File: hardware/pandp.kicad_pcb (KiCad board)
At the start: 2 copper layers, 116 x 55.5 mm, 93 parts, among them IC1 ADP2303-5, IC2 DRV8830, P1 CONN_01X02, P10 CONN_01X04, P11 CONN_01X02, P12 CONN_02X04, P13 CONN_01X02, P14 CONN_01X04, P15 CONN_01X04, P16 CONN_01X03, P17 CONN_01X03, P18 CONN_01X03, P19 CONN_01X03, P2 CONN_01X03, P20 CONN_01X03, P21 CONN_01X03, P22 CONN_02X03, P23 CONN_02X03, P24 CONN_02X03, P25 CONN_02X03, P26 CONN_01X03, P27 CONN_01X03, P28 CONN_01X03, P29 CONN_01X03, P3 CONN_01X02, P30 CONN_01X04, P31 CONN_01X04, P32 CONN_01X04, P33 CONN_01X04, P4 CONN_01X03, P5 CONN_01X02, P6 CONN_01X03, P7 CONN_01X03, P8 USB_OTG, P9 CONN_01X02, Q1 IRF540N, Q2 IRF540N, SW1 SW_PUSH, U1 AP1117D33, U2 STM32F103RC, Y1 Crystal_Small - 2101357 on el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, Y2 Crystal_Small - 2063972 on el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

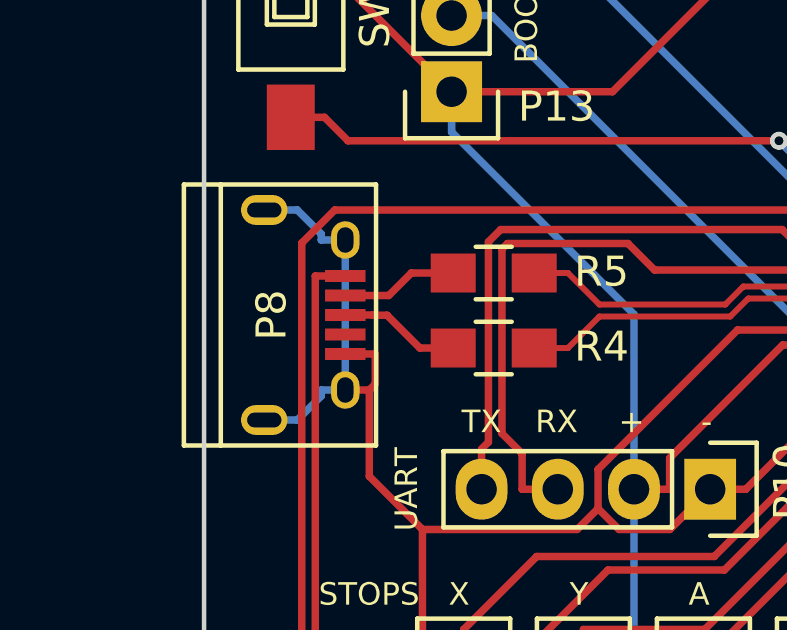
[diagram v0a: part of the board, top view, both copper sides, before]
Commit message: oshpark compatible holes for uusb connector
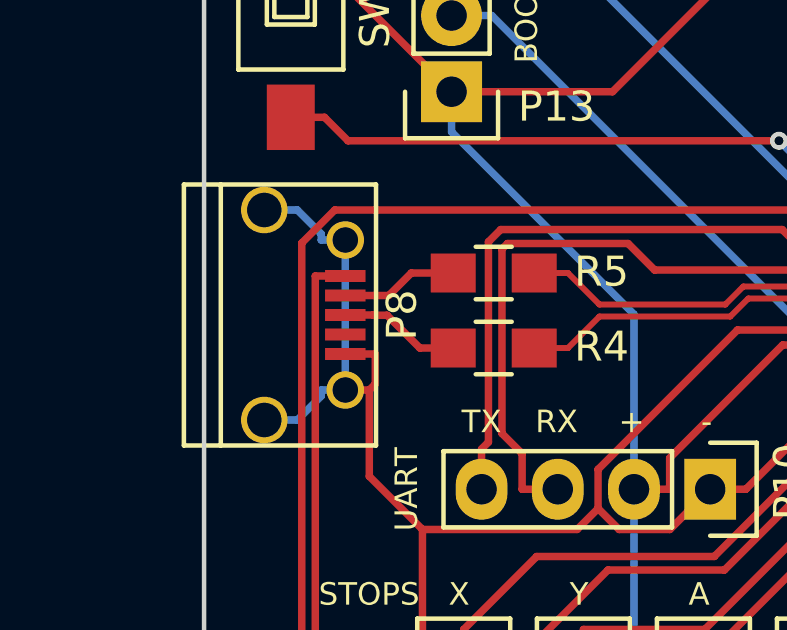
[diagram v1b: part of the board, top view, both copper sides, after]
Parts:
- P8: footprint Connect:USB_Micro-B -> MyLibs:USB_Micro-B-OshPark
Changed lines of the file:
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@@
     (links 267)
     (no_connects 0)
-    (area 82.424999 61.674999 198.575001 117.325001)
+    (area 77.775 50.367857 210.5 124.100001)
     (thickness 1.6)
     (drawings 78)
@@
     (36 B.SilkS user)
     (37 F.SilkS user)
-    (38 B.Mask user)
-    (39 F.Mask user)
+    (38 B.Mask user hide)
+    (39 F.Mask user hide)
     (40 Dwgs.User user)
     (41 Cmts.User user)
@@
     (add_net "Net-(IC2-Pad3)")
   )
-  (module Connect:USB_Micro-B (layer F.Cu)
-    (at 85.6447 97.693 270)
-    (descr "Micro USB Type B Receptacle")
-    (tags "USB USB_B USB_micro USB_OTG")
-    (attr smd)
-    (fp_text reference P8 (at 0 0.8947 270) (layer F.SilkS)
-      (effects (font (size 1 1) (thickness 0.15)))
-    )
-    (fp_text value USB_OTG (at 0 4.8 270) (layer F.Fab)
-      (effects (font (size 1 1) (thickness 0.15)))
-    )
-    (fp_line (start -4.6 -2.8) (end 4.6 -2.8) (layer F.CrtYd) (width 0.05))
-    (fp_line (start 4.6 -2.8) (end 4.6 4.05) (layer F.CrtYd) (width 0.05))
-    (fp_line (start 4.6 4.05) (end -4.6 4.05) (layer F.CrtYd) (width 0.05))
-    (fp_line (start -4.6 4.05) (end -4.6 -2.8) (layer F.CrtYd) (width 0.05))
-    (fp_line (start -4.3509 3.81746) (end 4.3491 3.81746) (layer F.SilkS) (width 0.15))
-    (fp_line (start -4.3509 -2.58754) (end 4.3491 -2.58754) (layer F.SilkS) (width 0.15))
-    (fp_line (start 4.3491 -2.58754) (end 4.3491 3.81746) (layer F.SilkS) (width 0.15))
-    (fp_line (start 4.3491 2.58746) (end -4.3509 2.58746) (layer F.SilkS) (width 0.15))
-    (fp_line (start -4.3509 3.81746) (end -4.3509 -2.58754) (layer F.SilkS) (width 0.15))
-    (pad 1 smd rect (at -1.3009 -1.56254) (size 1.35 0.4) (layers F.Cu F.Paste F.Mask)
-      (net 92 +5VL))
-    (pad 2 smd rect (at -0.6509 -1.56254) (size 1.35 0.4) (layers F.Cu F.Paste F.Mask)
-      (net 60 "Net-(P8-Pad2)"))
-    (pad 3 smd rect (at -0.0009 -1.56254) (size 1.35 0.4) (layers F.Cu F.Paste F.Mask)
-      (net 61 "Net-(P8-Pad3)"))
-    (pad 4 smd rect (at 0.6491 -1.56254) (size 1.35 0.4) (layers F.Cu F.Paste F.Mask))
-    (pad 5 smd rect (at 1.2991 -1.56254) (size 1.35 0.4) (layers F.Cu F.Paste F.Mask)
-      (net 90 GNDD))
-    (pad 6 thru_hole oval (at -2.5009 -1.56254) (size 0.95 1.25) (drill oval 0.55 0.85) (layers *.Cu *.Mask F.SilkS)
-      (net 90 GNDD))
-    (pad 6 thru_hole oval (at 2.4991 -1.56254) (size 0.95 1.25) (drill oval 0.55 0.85) (layers *.Cu *.Mask F.SilkS)
-      (net 90 GNDD))
-    (pad 6 thru_hole oval (at -3.5009 1.13746) (size 1.55 1) (drill oval 1.15 0.5) (layers *.Cu *.Mask F.SilkS)
-      (net 90 GNDD))
-    (pad 6 thru_hole oval (at 3.4991 1.13746) (size 1.55 1) (drill oval 1.15 0.5) (layers *.Cu *.Mask F.SilkS)
-      (net 90 GNDD))
-  )
   (module SMD_Packages:SMD-1210_Pol (layer F.Cu)
     (at 186.75 89.222 270)
@@
     )
   )
+  (module MyLibs:USB_Micro-B-OshPark (layer F.Cu)
+    (at 85.6447 97.693 270)
+    (descr "Micro USB Type B Receptacle")
+    (tags "USB USB_B USB_micro USB_OTG")
+    (attr smd)
+    (fp_text reference P8 (at 0 -3.45 270) (layer F.SilkS)
+      (effects (font (size 1 1) (thickness 0.15)))
+    )
+    (fp_text value USB_OTG (at 0 4.8 270) (layer F.Fab)
+      (effects (font (size 1 1) (thickness 0.15)))
+    )
+    (fp_line (start -4.6 -2.8) (end 4.6 -2.8) (layer F.CrtYd) (width 0.05))
+    (fp_line (start 4.6 -2.8) (end 4.6 4.05) (layer F.CrtYd) (width 0.05))
+    (fp_line (start 4.6 4.05) (end -4.6 4.05) (layer F.CrtYd) (width 0.05))
+    (fp_line (start -4.6 4.05) (end -4.6 -2.8) (layer F.CrtYd) (width 0.05))
+    (fp_line (start -4.3509 3.81746) (end 4.3491 3.81746) (layer F.SilkS) (width 0.15))
+    (fp_line (start -4.3509 -2.58754) (end 4.3491 -2.58754) (layer F.SilkS) (width 0.15))
+    (fp_line (start 4.3491 -2.58754) (end 4.3491 3.81746) (layer F.SilkS) (width 0.15))
+    (fp_line (start 4.3491 2.58746) (end -4.3509 2.58746) (layer F.SilkS) (width 0.15))
+    (fp_line (start -4.3509 3.81746) (end -4.3509 -2.58754) (layer F.SilkS) (width 0.15))
+    (pad 1 smd rect (at -1.3009 -1.56254) (size 1.35 0.4) (layers F.Cu F.Paste F.Mask)
+      (net 92 +5VL))
+    (pad 2 smd rect (at -0.6509 -1.56254) (size 1.35 0.4) (layers F.Cu F.Paste F.Mask)
+      (net 60 "Net-(P8-Pad2)"))
+    (pad 3 smd rect (at -0.0009 -1.56254) (size 1.35 0.4) (layers F.Cu F.Paste F.Mask)
+      (net 61 "Net-(P8-Pad3)"))
+    (pad 4 smd rect (at 0.6491 -1.56254) (size 1.35 0.4) (layers F.Cu F.Paste F.Mask))
+    (pad 5 smd rect (at 1.2991 -1.56254) (size 1.35 0.4) (layers F.Cu F.Paste F.Mask)
+      (net 90 GNDD))
+    (pad 6 thru_hole circle (at -2.5009 -1.56254) (size 1.25 1.25) (drill 0.85) (layers *.Cu *.Mask F.SilkS)
+      (net 90 GNDD))
+    (pad 6 thru_hole circle (at 2.4991 -1.56254) (size 1.25 1.25) (drill 0.85) (layers *.Cu *.Mask F.SilkS)
+      (net 90 GNDD))
+    (pad 6 thru_hole circle (at -3.5009 1.13746) (size 1.55 1.55) (drill 1.15) (layers *.Cu *.Mask F.SilkS)
+      (net 90 GNDD))
+    (pad 6 thru_hole circle (at 3.4991 1.13746) (size 1.55 1.55) (drill 1.15) (layers *.Cu *.Mask F.SilkS)
+      (net 90 GNDD))
+  )
   (gr_text DC01 (at 141 116.5) (layer F.SilkS)

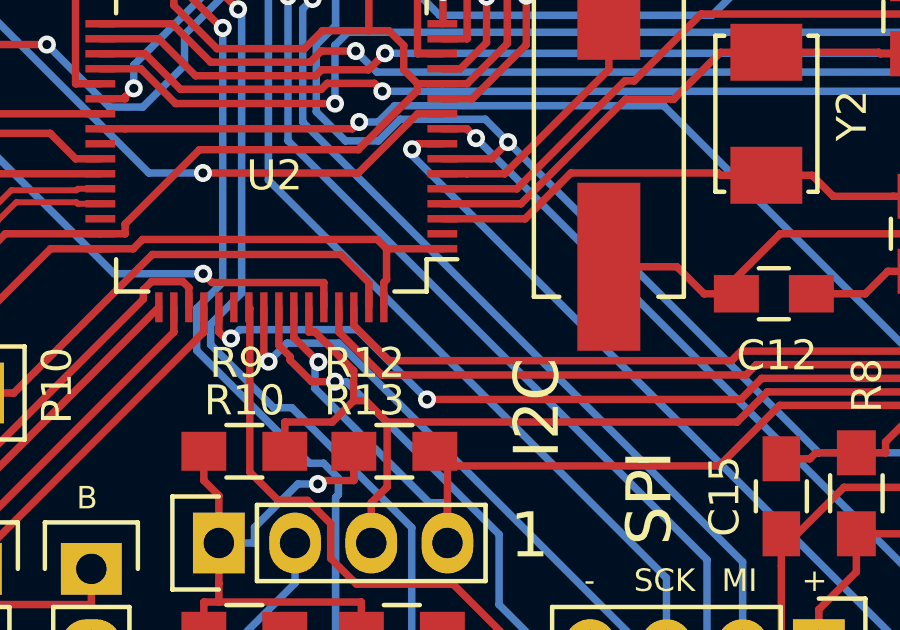
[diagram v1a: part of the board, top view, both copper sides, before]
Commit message: new uusb oshpark compatible, added a mark for the stm chip pin 0
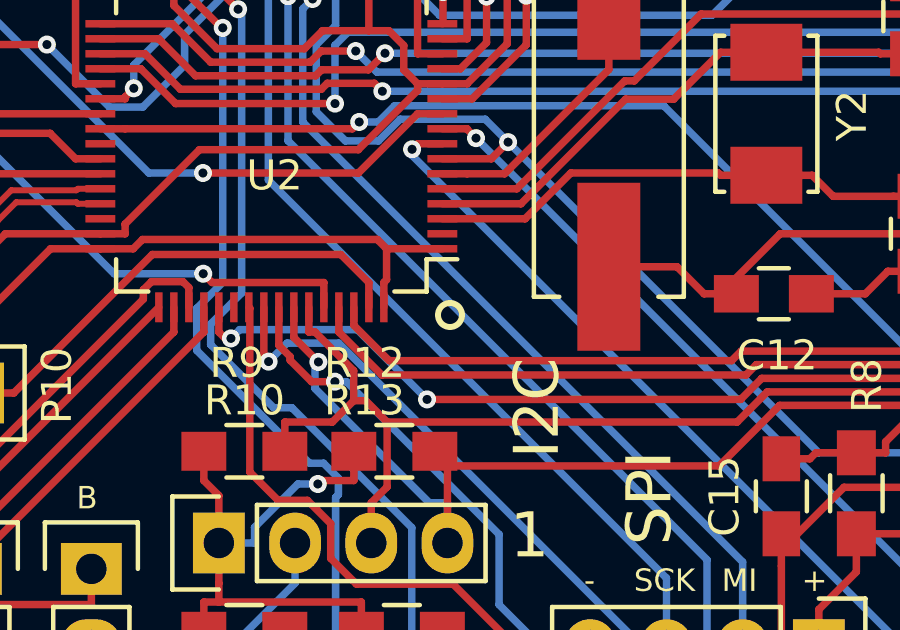
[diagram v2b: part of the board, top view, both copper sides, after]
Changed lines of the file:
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@@
     (links 267)
     (no_connects 0)
-    (area 77.775 50.367857 210.5 124.100001)
+    (area 82.424999 61.674999 198.575001 117.325001)
     (thickness 1.6)
-    (drawings 78)
+    (drawings 79)
     (tracks 1240)
     (zones 0)
@@
     (36 B.SilkS user)
     (37 F.SilkS user)
-    (38 B.Mask user hide)
-    (39 F.Mask user hide)
+    (38 B.Mask user)
+    (39 F.Mask user)
     (40 Dwgs.User user)
     (41 Cmts.User user)
@@
       (net 90 GNDD))
   )
+  (gr_circle (center 115.1 100.9) (end 115.1 101.3) (layer F.SilkS) (width 0.2))
   (gr_text DC01 (at 141 116.5) (layer F.SilkS)
     (effects (font (size 0.75 0.75) (thickness 0.1875)))
